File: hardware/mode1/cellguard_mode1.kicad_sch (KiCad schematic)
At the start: 22 parts, among them J1 Raspberry Pi 5 GPIO Header, J2 ZY12PDN PD Trigger (5V), J3 ATORCH BW150 부하 입력, K1 4CH Relay [SZH-RLBG-012], U1 INA226 [VLT-VCM029], U2 Battery Babysitter [PRT-13777], U3 MLX90614 #1 (0x5A, 셀 중앙), U4 ADS1115 [VLT-AD004], U5 DS18B20 #1 (셀 하단), U6 OLED 0.96in SPI [CN0219], U7 DS18B20 #2 (셀 중앙), U8 DS18B20 #3 (셀 상단·단자쪽), U9 MLX90614 #2 (0x5B, 셀 단자쪽)

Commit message: fix(hw): 모드 1 회로에서 F1 폴리퓨즈 제거 — 과전류 보호를 셀 보호회로에 위임
F1은 회로도를 그리며 넣은 부품인데 PLAN.md의 구매 확정 목록에도,
미확보 목록에도 없었다("퓨즈" 0건). 새로 사지 않고 회로에서 뺀다.

회로 (정본)
- gen_mode1_sch.py: POLYFUSE 심볼·F1 인스턴스 삭제. CELL_P_F 네트가
  사라지고 셀 +는 CELL_P 한 노드로 INA226 IN-·VBUS에 직결된다.
- 재생성 후 ERC 위반 0건, SVG 재출력. 네트리스트로 CELL_P = BT1.+ /
  U1.IN- / U1.VBUS 확인, CELL_P_F 0건 확인.

이 결정의 대가 — 회로 안에 과전류를 막을 소자가 하나도 없다
- 가이드 §3에 `⑥ 셀에 보호회로(PCM)가 붙어 있는가` 추가 (5가지 -> 6가지).
  protected/unprotected 구분법(18650 68~70mm vs 65mm, 파우치의 기판 유무),
  없으면 셀 교체 또는 폴리퓨즈 신규 구매.
- §5 3단계 셀 삽입 직전 검사에 보호회로 확인 추가.
- §7에 14번 "보호회로 없는 맨 셀을 물림" 추가 (13가지 -> 14가지).
- §2 BT1 행, §4-3 전력 경로에 경고 명시.

문서 정리
- §1 전류 경로 그림 2장에서 F1 제거. §4-3 CELL_P/CELL_P_F 두 행을 한 행으로.
  §9 폴리퓨즈 항목 삭제. §10 인계 목록에 보호회로 유무·실측 길이 추가.
- 백엔드 스펙 §3-5의 "퓨즈 앞" 표현 정정.
- CLAUDE.md: 직전 커밋에 넣은 "VBUS는 퓨즈 앞" 항목을 무퓨즈 정책으로 교체.
- PLAN.md: 변경 이력 2026-07-28 항목 신설, 하드웨어 제약에 무퓨즈 명시.

미해결 (PLAN.md `정의 필요`로 등록)
- 구매한 18650[ZM18650-2600-KC01]·리튬폴리머[TW102050]에 보호회로가
  실제로 있는지 실물 미확인. 없으면 이 결정의 전제가 깨진다.
- 보호회로가 있으면 18650이 68~70mm라 홀더 규격과 §4-5 DS18B20 3점
  배치 치수가 달라진다.

Co-Authored-By: Claude Opus 5 <noreply@anthropic.com>
Claude-Session: https://claude.ai/code/session_01JTJvnafHr2vM6f9oKrnscb
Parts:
- removed F1: PolyFuse 3A, symbol cellguard:POLYFUSE
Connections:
- net CELL_P_F is gone; now on net CELL_P: U1.2 (IN-)
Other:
- note added: "18650 홀더, JST 2.0 커넥터, 4.7k/10k 저항,"
- note added: "[!] 직렬 퓨즈 없음. 과전류 보호는 셀에 붙은 보호회로(PCM)에만 의존한다."
- note added: "보호회로 없는 맨 셀(unprotected)을 물리면 배선 단락 시 아무 보호도 없다 — 실물 확인 필수."
- note added: "충전: ZY12PDN 5V -[CH1]- Babysitter VIN -> (BQ24075) -> BAT+ -[CH3]- INA226 션트 - 셀 +"
- note removed: "전압 탭: INA226 VBUS는 퓨즈 앞(CELL_P)에서 딴다. 퓨즈 뒤면 폴리퓨즈 저항만큼 깎인다."
- note removed: "충전: ZY12PDN 5V -[CH1]- Babysitter VIN -> (BQ24075) -> BAT+ -[CH3]- INA226 션트 - F1 - 셀 +"
- note removed: "폴리퓨즈 3A, 18650 홀더, JST 2.0 커넥터, 4.7k/10k 저항,"
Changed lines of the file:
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@@
-	)
-	(symbol
-		(lib_id "cellguard:POLYFUSE")
-		(at 62.23 72.39 0)
-		(unit 1)
-		(exclude_from_sim no)
-		(in_bom yes)
-		(on_board yes)
-		(dnp no)
-		(property "Reference" "F1" (at 52.07 63.50 0) (effects (font (face "Apple SD Gothic Neo") (size 1.27 1.27)) (justify left bottom)))
-		(property "Value" "PolyFuse 3A" (at 52.07 66.04 0) (effects (font (face "Apple SD Gothic Neo") (size 1.27 1.27)) (justify left bottom)))
-		(property "Footprint" "" (at 62.23 72.39 0) (effects (font (face "Apple SD Gothic Neo") (size 1.27 1.27)) (hide yes)))
-		(property "Datasheet" "" (at 62.23 72.39 0) (effects (font (face "Apple SD Gothic Neo") (size 1.27 1.27)) (hide yes)))
-		(property "Description" "셀 + 경로 과전류 보호 (미확보 — 조립 전 확보 필요)" (at 62.23 72.39 0) (effects (font (face "Apple SD Gothic Neo") (size 1.27 1.27)) (hide yes)))
-		(instances
-			(project "cellguard_mode1"
-				(path "/2591c9a4-08c7-5581-87ba-34dbe85f198c" (reference "F1") (unit 1))
-			)
-		)
-	)
-	(wire
-		(pts (xy 46.99 72.39) (xy 41.91 72.39))
-		(stroke (width 0) (type default))
-	)
-	(global_label "CELL_P"
-		(shape bidirectional)
-		(at 41.91 72.39 180)
-		(effects (font (face "Apple SD Gothic Neo") (size 1.27 1.27)) (justify right))
-		(property "Intersheetrefs" "${INTERSHEET_REFS}" (at 0 0 0) (effects (font (face "Apple SD Gothic Neo") (size 1.27 1.27)) (hide yes)))
-	)
-	(wire
-		(pts (xy 77.47 72.39) (xy 82.55 72.39))
-		(stroke (width 0) (type default))
-	)
-	(global_label "CELL_P_F"
-		(shape bidirectional)
-		(at 82.55 72.39 0)
-		(effects (font (face "Apple SD Gothic Neo") (size 1.27 1.27)) (justify left))
-		(property "Intersheetrefs" "${INTERSHEET_REFS}" (at 0 0 0) (effects (font (face "Apple SD Gothic Neo") (size 1.27 1.27)) (hide yes)))
 	)
 	(symbol
@@
 		(stroke (width 0) (type default))
 	)
-	(global_label "CELL_P_F"
+	(global_label "CELL_P"
 		(shape bidirectional)
 		(at 35.56 113.03 180)
@@
 		(effects (font (face "Apple SD Gothic Neo") (size 3.0 3.0)) (justify left bottom))
 	)
-	(text "충전:  ZY12PDN 5V -[CH1]- Babysitter VIN -> (BQ24075) -> BAT+ -[CH3]- INA226 션트 - F1 - 셀 +"
+	(text "충전:  ZY12PDN 5V -[CH1]- Babysitter VIN -> (BQ24075) -> BAT+ -[CH3]- INA226 션트 - 셀 +"
 		(exclude_from_sim no)
 		(at 20.00 314.00 0)
 		(effects (font (face "Apple SD Gothic Neo") (size 2.0 2.0)) (justify left bottom))
 	)
-	(text "전압 탭:  INA226 VBUS는 퓨즈 앞(CELL_P)에서 딴다. 퓨즈 뒤면 폴리퓨즈 저항만큼 깎인다."
+	(text "[!] 직렬 퓨즈 없음.  과전류 보호는 셀에 붙은 보호회로(PCM)에만 의존한다."
 		(exclude_from_sim no)
 		(at 20.00 319.20 0)
 		(effects (font (face "Apple SD Gothic Neo") (size 2.0 2.0)) (justify left bottom))
 	)
+	(text "    보호회로 없는 맨 셀(unprotected)을 물리면 배선 단락 시 아무 보호도 없다 — 실물 확인 필수."
+		(exclude_from_sim no)
+		(at 20.00 324.40 0)
+		(effects (font (face "Apple SD Gothic Neo") (size 2.0 2.0)) (justify left bottom))
+	)
 	(text "방전:  셀 + -> ... -> Babysitter SYS+ -[CH2]- ATORCH BW150 부하 +"
 		(exclude_from_sim no)
-		(at 20.00 324.40 0)
+		(at 20.00 329.60 0)
 		(effects (font (face "Apple SD Gothic Neo") (size 2.0 2.0)) (justify left bottom))
 	)
 	(text "부호 규약:  INA226 IN+ -> IN- 방향(릴레이 -> 셀)이 양수 = 충전.  방전은 음수."
 		(exclude_from_sim no)
-		(at 20.00 329.60 0)
+		(at 20.00 334.80 0)
 		(effects (font (face "Apple SD Gothic Neo") (size 2.0 2.0)) (justify left bottom))
 	)
 	(text "[!] 조립 전 반드시 확인 — 여기서 틀리면 부품이 탄다"
 		(exclude_from_sim no)
-		(at 20.00 337.80 0)
+		(at 20.00 343.00 0)
 		(effects (font (face "Apple SD Gothic Neo") (size 2.5 2.5)) (justify left bottom))
 	)
 	(text "1. ZY12PDN을 5V로 설정했는가.  9V/12V면 Babysitter가 즉시 파손된다."
 		(exclude_from_sim no)
-		(at 20.00 345.80 0)
+		(at 20.00 351.00 0)
 		(effects (font (face "Apple SD Gothic Neo") (size 2.0 2.0)) (justify left bottom))
 	)
 	(text "2. 릴레이 VCC-JD_VCC 점퍼를 뽑았는가.  VCC=Pi 3.3V(옵토측), JD_VCC=5V(코일측)."
 		(exclude_from_sim no)
-		(at 20.00 351.00 0)
+		(at 20.00 356.20 0)
 		(effects (font (face "Apple SD Gothic Neo") (size 2.0 2.0)) (justify left bottom))
 	)
 	(text "   점퍼를 꽂아 두면 VCC=5V가 되어 3.3V 로직으로 옵토 LED를 확실히 끄지 못한다."
 		(exclude_from_sim no)
-		(at 20.00 356.20 0)
+		(at 20.00 361.40 0)
 		(effects (font (face "Apple SD Gothic Neo") (size 2.0 2.0)) (justify left bottom))
 	)
 	(text "3. INA226 보드의 션트 저항값을 실크스크린에서 읽었는가."
 		(exclude_from_sim no)
-		(at 20.00 361.40 0)
+		(at 20.00 366.60 0)
 		(effects (font (face "Apple SD Gothic Neo") (size 2.0 2.0)) (justify left bottom))
 	)
 	(text "   R100=0.1ohm / R010=0.01ohm / R002=0.002ohm -> Calibration 레지스터 값이 달라진다."
 		(exclude_from_sim no)
-		(at 20.00 366.60 0)
+		(at 20.00 371.80 0)
 		(effects (font (face "Apple SD Gothic Neo") (size 2.0 2.0)) (justify left bottom))
 	)
 	(text "   전류 측정 상한은 션트가 아니라 16비트 Current 레지스터가 정한다 -> 기본 설정에서 3.28A."
 		(exclude_from_sim no)
-		(at 20.00 371.80 0)
+		(at 20.00 377.00 0)
 		(effects (font (face "Apple SD Gothic Neo") (size 2.0 2.0)) (justify left bottom))
 	)
 	(text "4. 셀 -(음극)를 시스템 GND에 직접 연결하지 마라."
 		(exclude_from_sim no)
-		(at 20.00 377.00 0)
+		(at 20.00 382.20 0)
 		(effects (font (face "Apple SD Gothic Neo") (size 2.0 2.0)) (justify left bottom))
 	)
 	(text "   CELL_N은 Babysitter BAT- 하나에만 간다. BQ27441의 20mohm 센스 저항이"
 		(exclude_from_sim no)
-		(at 20.00 382.20 0)
+		(at 20.00 387.40 0)
 		(effects (font (face "Apple SD Gothic Neo") (size 2.0 2.0)) (justify left bottom))
 	)
 	(text "   BAT-와 GND 사이에 있어서, 직결하면 이 저항이 단락되고 SOC가 안 나온다."
 		(exclude_from_sim no)
-		(at 20.00 387.40 0)
+		(at 20.00 392.60 0)
 		(effects (font (face "Apple SD Gothic Neo") (size 2.0 2.0)) (justify left bottom))
 	)
 	(text "[!] 릴레이는 active-LOW다"
 		(exclude_from_sim no)
-		(at 20.00 395.60 0)
+		(at 20.00 400.80 0)
 		(effects (font (face "Apple SD Gothic Neo") (size 2.5 2.5)) (justify left bottom))
 	)
 	(text "GPIO=0 -> 접점 붙음(도통) / GPIO=1 -> 접점 떨어짐(차단)."
 		(exclude_from_sim no)
-		(at 20.00 403.60 0)
+		(at 20.00 408.80 0)
 		(effects (font (face "Apple SD Gothic Neo") (size 2.0 2.0)) (justify left bottom))
 	)
 	(text "모든 배터리 경로가 NO 접점을 지나므로 정전 / 부팅 중 / 크래시 = 자동 차단(fail-safe)."
 		(exclude_from_sim no)
-		(at 20.00 408.80 0)
+		(at 20.00 414.00 0)
 		(effects (font (face "Apple SD Gothic Neo") (size 2.0 2.0)) (justify left bottom))
 	)
 	(text "부팅 초기 보호 2중화:  IN1~IN4에 10k 풀업(R3~R6)"
 		(exclude_from_sim no)
-		(at 20.00 414.00 0)
+		(at 20.00 419.20 0)
 		(effects (font (face "Apple SD Gothic Neo") (size 2.0 2.0)) (justify left bottom))
 	)
 	(text "                        + /boot/firmware/config.txt 에 gpio=5,6,13,19=op,dh"
 		(exclude_from_sim no)
-		(at 20.00 419.20 0)
+		(at 20.00 424.40 0)
 		(effects (font (face "Apple SD Gothic Neo") (size 2.0 2.0)) (justify left bottom))
 	)
 	(text "  ※ config.txt 쪽은 Pi 5 에서 안 먹을 수 있다. 전원 인가 순간부터 확실한 건 10k 풀업뿐이니"
 		(exclude_from_sim no)
-		(at 20.00 424.40 0)
+		(at 20.00 429.60 0)
 		(effects (font (face "Apple SD Gothic Neo") (size 2.0 2.0)) (justify left bottom))
 	)
 	(text "     R3~R6 을 절대 생략하지 마라.  재부팅 후 pinctrl get 5,6,13,19 으로 확인할 것."
 		(exclude_from_sim no)
-		(at 20.00 429.60 0)
+		(at 20.00 434.80 0)
 		(effects (font (face "Apple SD Gothic Neo") (size 2.0 2.0)) (justify left bottom))
 	)
@@
 		(effects (font (face "Apple SD Gothic Neo") (size 2.5 2.5)) (justify left bottom))
 	)
-	(text "폴리퓨즈 3A, 18650 홀더, JST 2.0 커넥터, 4.7k/10k 저항,"
+	(text "18650 홀더, JST 2.0 커넥터, 4.7k/10k 저항,"
 		(exclude_from_sim no)
 		(at 580.00 408.80 0)

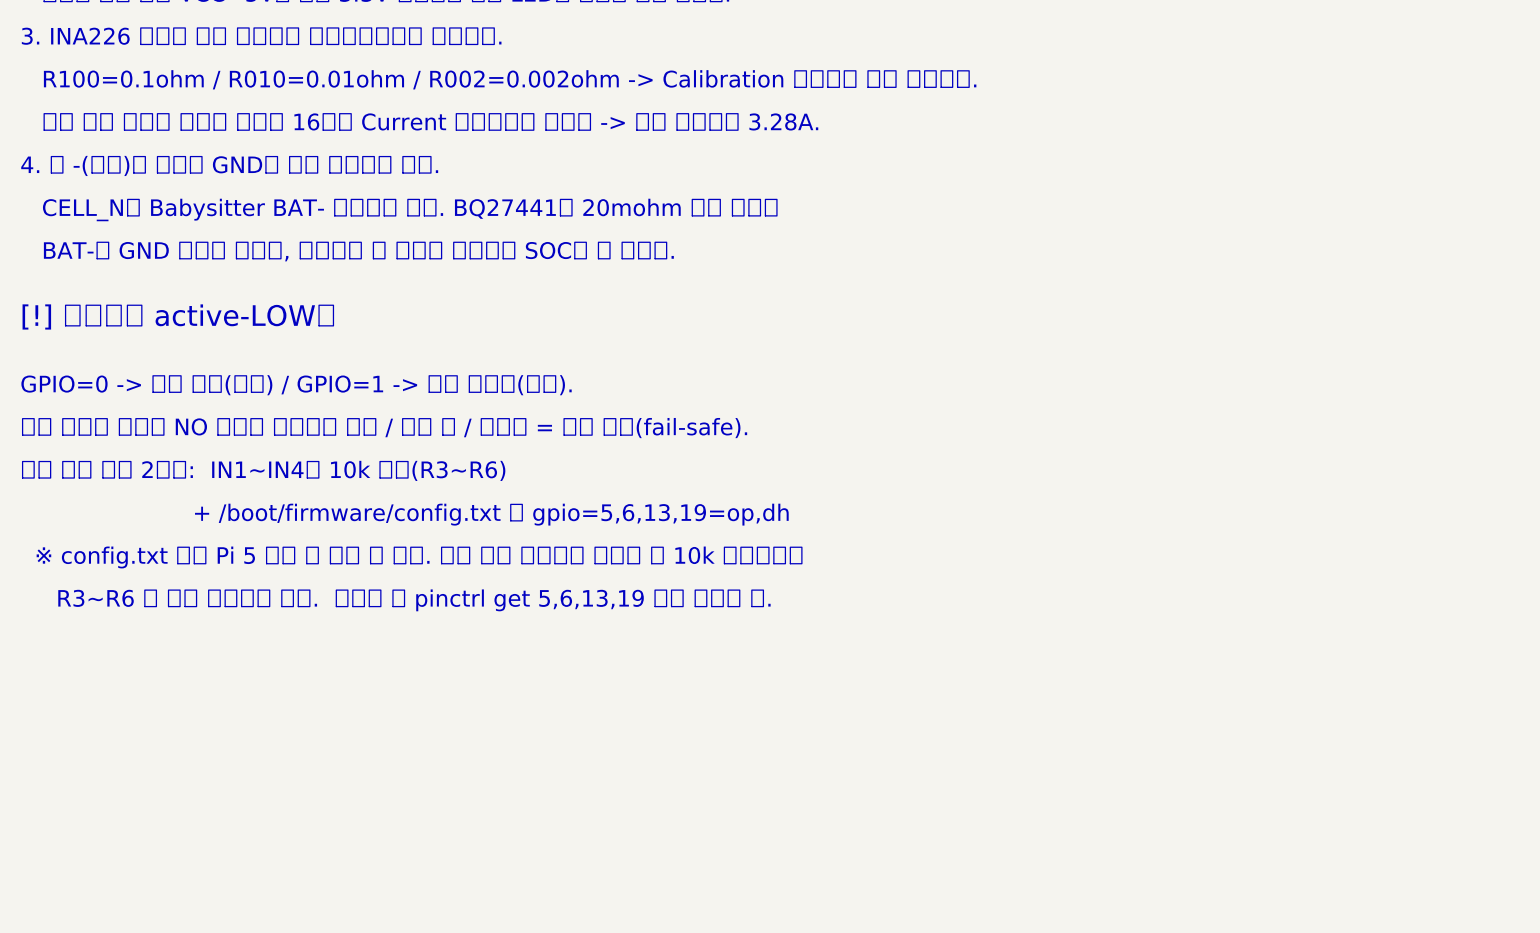
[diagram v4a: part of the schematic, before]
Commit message: docs(hw): SparkFun 공식 회로도로 Babysitter 관련 오류 3건 정정
`bq24075` 데이터시트와 Battery Babysitter v10 공식 회로도를 대조한 결과,
문서가 사실과 다른 곳이 세 군데 있었다.

1. 센스 저항 위치가 반대였다
   `R11`(0.01Ω)은 배터리 `−`↔GND가 아니라 배터리 `+` 쪽 하이사이드
   (`BATTERY_IN`↔`V_BATT`)에 있고, 배터리 `−`는 보드 `GND`에 직결이다.
   - "셀 −를 GND에 물리면 SOC가 죽는다" → 사실 아님. `CELL_N`↔GND 도통은 정상
   - STEP 24의 `CELL_N` 격리 도통 검사는 멀쩡한 배선을 불합격시킨다 → 육안 검사로 교체
   - 백엔드 스펙 §3-5의 `voltage_v` 20mΩ 보정식은 없는 오차를 3A에서 60mV씩
     주입한다 → 폐기. 남는 건 배선 IR 강하뿐이라 계산 보정 불가
   - `CELL_N`을 한 점에만 무는 규칙 자체는 유지(스타 그라운드). 배선 변경 없음
   - §13 H5를 "센스 저항 역산"에서 "귀환 경로 IR 강하 실측"으로 교체

2. 보드 실크스크린이 회로도 네트 이름과 같다는 기록이 틀렸다
   `GND_IN`·`SYS+`·`SYS−`·`BAT+`·`BAT−`는 보드에 없는 글자다.
   STEP 3에 대응표 추가 — `VIN −` / `VOUT +` / `VOUT −` / JST `+` / JST `−`,
   네모 패드가 있는 줄이 `+`, 한 줄의 3구멍은 같은 네트(`JP2~4`·`JP7~9` 병렬).
   `GND`·`GND_IN`·`SYS−`가 보드 안에서 같은 네트임도 명시.

3. 온보드 스위치 2개가 가이드에 아예 없었다 (§2-⑥ 신설)
   - `S1` 슬라이드 = `SYSOFF`(active-high, HIGH=OFF) — `OFF`면 `SYS+` 출력 0
   - `S2` DIP = `EN1`/`EN2`, 10k로 `OUT` 풀업 — 출고 기본 `1,1`은 Standby(충전 안 함).
     설정값 `EN2=1, EN1=0`
   - `R5`=590Ω → `I_CHG`≈1.5A, `R7`=1.1kΩ → `I_INMAX`≈1.5A.
     2550mAh 18650에 0.59C라 셀 스펙 확인 항목 추가

회로도 심볼 설명과 주석에도 반영하고 재생성(ERC 위반 0건).

Co-Authored-By: Claude Opus 5 <noreply@anthropic.com>
Claude-Session: https://claude.ai/code/session_01TdBrQJ3tYNhWGCkoy4xU7s
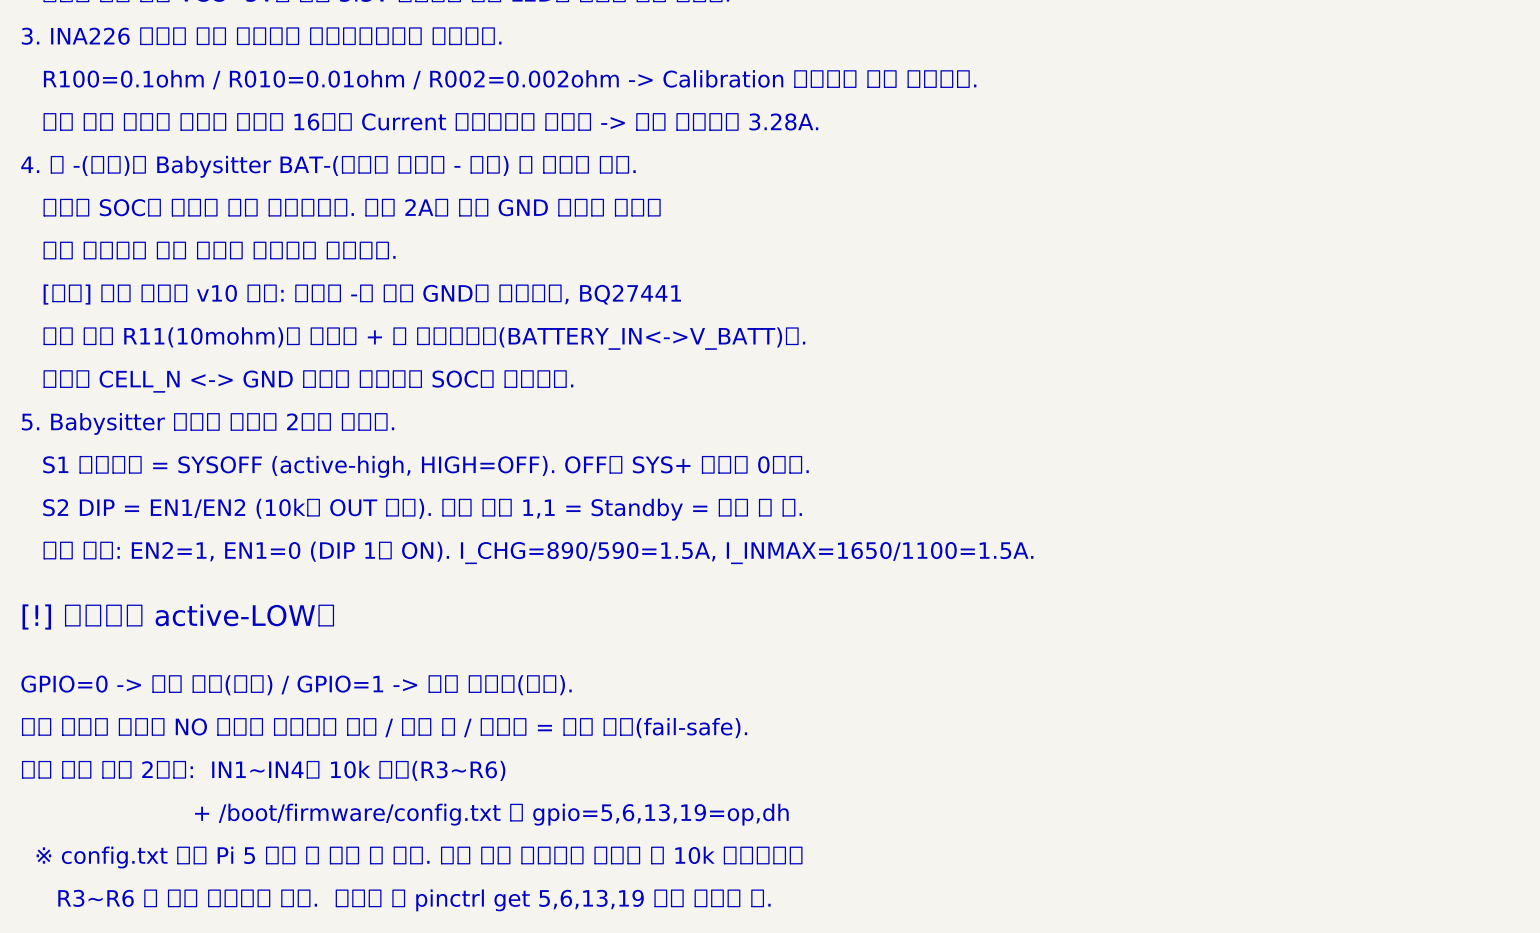
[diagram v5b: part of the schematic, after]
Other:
- note added: "4. 셀 -(음극)는 Babysitter BAT-(보드의 배터리 - 단자) 한 점에만 문다."
- note added: "5. Babysitter 온보드 스위치 2개를 맞춰라."
- note added: "S1 슬라이드 = SYSOFF (active-high, HIGH=OFF). OFF면 SYS+ 출력이 0이다."
- note added: "S2 DIP = EN1/EN2 (10k로 OUT 풀업). 출고 기본 1,1 = Standby = 충전 안 함."
- note added: "[주의] 공식 회로도 v10 확인: 배터리 -는 보드 GND에 직결이고, BQ27441"
- note added: "따라서 CELL_N <-> GND 도통은 정상이며 SOC와 무관하다."
- note added: "센스 저항 R11(10mohm)은 배터리 + 쪽 하이사이드(BATTERY_IN<->V_BATT)다."
- note added: "우리 설정: EN2=1, EN1=0 (DIP 1만 ON). I_CHG=890/590=1.5A, I_INMAX=1650/1100=1.5A."
- note added: "이유는 SOC가 아니라 스타 그라운드다. 방전 2A가 신호 GND 레일을 지나면"
- note added: "전압 강하만큼 모든 센서의 기준점이 흔들린다."
- note removed: "4. 셀 -(음극)를 시스템 GND에 직접 연결하지 마라."
- note removed: "BAT-와 GND 사이에 있어서, 직결하면 이 저항이 단락되고 SOC가 안 나온다."
- note removed: "CELL_N은 Babysitter BAT- 하나에만 간다. BQ27441의 20mohm 센스 저항이"
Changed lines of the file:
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@@
 		(property "Footprint" "" (at 219.71 167.64 0) (effects (font (face "Apple SD Gothic Neo") (size 1.27 1.27)) (hide yes)))
 		(property "Datasheet" "" (at 219.71 167.64 0) (effects (font (face "Apple SD Gothic Neo") (size 1.27 1.27)) (hide yes)))
-		(property "Description" "BQ24075 충전기 + BQ27441 퓨얼게이지(SOC), I2C 0x55" (at 219.71 167.64 0) (effects (font (face "Apple SD Gothic Neo") (size 1.27 1.27)) (hide yes)))
+		(property "Description" "BQ24075 충전기 + BQ27441 퓨얼게이지(SOC), I2C 0x55. 핀 이름은 회로도 규약이며 보드 실크스크린과 다르다 -- VIN/GND_IN=VIN +/-, SYS+/SYS-=VOUT +/-, BAT+/BAT-=JST +/-. GND/GND_IN/SYS-는 보드 안에서 같은 GND 네트" (at 219.71 167.64 0) (effects (font (face "Apple SD Gothic Neo") (size 1.27 1.27)) (hide yes)))
 		(instances
 			(project "cellguard_mode1"
@@
 		(effects (font (face "Apple SD Gothic Neo") (size 2.0 2.0)) (justify left bottom))
 	)
-	(text "4. 셀 -(음극)를 시스템 GND에 직접 연결하지 마라."
+	(text "4. 셀 -(음극)는 Babysitter BAT-(보드의 배터리 - 단자) 한 점에만 문다."
 		(exclude_from_sim no)
 		(at 20.00 382.20 0)
 		(effects (font (face "Apple SD Gothic Neo") (size 2.0 2.0)) (justify left bottom))
 	)
-	(text "   CELL_N은 Babysitter BAT- 하나에만 간다. BQ27441의 20mohm 센스 저항이"
+	(text "   이유는 SOC가 아니라 스타 그라운드다. 방전 2A가 신호 GND 레일을 지나면"
 		(exclude_from_sim no)
 		(at 20.00 387.40 0)
 		(effects (font (face "Apple SD Gothic Neo") (size 2.0 2.0)) (justify left bottom))
 	)
-	(text "   BAT-와 GND 사이에 있어서, 직결하면 이 저항이 단락되고 SOC가 안 나온다."
+	(text "   전압 강하만큼 모든 센서의 기준점이 흔들린다."
 		(exclude_from_sim no)
 		(at 20.00 392.60 0)
 		(effects (font (face "Apple SD Gothic Neo") (size 2.0 2.0)) (justify left bottom))
 	)
+	(text "   [주의] 공식 회로도 v10 확인: 배터리 -는 보드 GND에 직결이고, BQ27441"
+		(exclude_from_sim no)
+		(at 20.00 397.80 0)
+		(effects (font (face "Apple SD Gothic Neo") (size 2.0 2.0)) (justify left bottom))
+	)
+	(text "   센스 저항 R11(10mohm)은 배터리 + 쪽 하이사이드(BATTERY_IN<->V_BATT)다."
+		(exclude_from_sim no)
+		(at 20.00 403.00 0)
+		(effects (font (face "Apple SD Gothic Neo") (size 2.0 2.0)) (justify left bottom))
+	)
+	(text "   따라서 CELL_N <-> GND 도통은 정상이며 SOC와 무관하다."
+		(exclude_from_sim no)
+		(at 20.00 408.20 0)
+		(effects (font (face "Apple SD Gothic Neo") (size 2.0 2.0)) (justify left bottom))
+	)
+	(text "5. Babysitter 온보드 스위치 2개를 맞춰라."
+		(exclude_from_sim no)
+		(at 20.00 413.40 0)
+		(effects (font (face "Apple SD Gothic Neo") (size 2.0 2.0)) (justify left bottom))
+	)
+	(text "   S1 슬라이드 = SYSOFF (active-high, HIGH=OFF). OFF면 SYS+ 출력이 0이다."
+		(exclude_from_sim no)
+		(at 20.00 418.60 0)
+		(effects (font (face "Apple SD Gothic Neo") (size 2.0 2.0)) (justify left bottom))
+	)
+	(text "   S2 DIP = EN1/EN2 (10k로 OUT 풀업). 출고 기본 1,1 = Standby = 충전 안 함."
+		(exclude_from_sim no)
+		(at 20.00 423.80 0)
+		(effects (font (face "Apple SD Gothic Neo") (size 2.0 2.0)) (justify left bottom))
+	)
+	(text "   우리 설정: EN2=1, EN1=0 (DIP 1만 ON). I_CHG=890/590=1.5A, I_INMAX=1650/1100=1.5A."
+		(exclude_from_sim no)
+		(at 20.00 429.00 0)
+		(effects (font (face "Apple SD Gothic Neo") (size 2.0 2.0)) (justify left bottom))
+	)
 	(text "[!] 릴레이는 active-LOW다"
 		(exclude_from_sim no)
-		(at 20.00 400.80 0)
+		(at 20.00 437.20 0)
 		(effects (font (face "Apple SD Gothic Neo") (size 2.5 2.5)) (justify left bottom))
 	)
 	(text "GPIO=0 -> 접점 붙음(도통) / GPIO=1 -> 접점 떨어짐(차단)."
 		(exclude_from_sim no)
-		(at 20.00 408.80 0)
+		(at 20.00 445.20 0)
 		(effects (font (face "Apple SD Gothic Neo") (size 2.0 2.0)) (justify left bottom))
 	)
 	(text "모든 배터리 경로가 NO 접점을 지나므로 정전 / 부팅 중 / 크래시 = 자동 차단(fail-safe)."
 		(exclude_from_sim no)
-		(at 20.00 414.00 0)
+		(at 20.00 450.40 0)
 		(effects (font (face "Apple SD Gothic Neo") (size 2.0 2.0)) (justify left bottom))
 	)
 	(text "부팅 초기 보호 2중화:  IN1~IN4에 10k 풀업(R3~R6)"
 		(exclude_from_sim no)
-		(at 20.00 419.20 0)
+		(at 20.00 455.60 0)
 		(effects (font (face "Apple SD Gothic Neo") (size 2.0 2.0)) (justify left bottom))
 	)
 	(text "                        + /boot/firmware/config.txt 에 gpio=5,6,13,19=op,dh"
 		(exclude_from_sim no)
-		(at 20.00 424.40 0)
+		(at 20.00 460.80 0)
 		(effects (font (face "Apple SD Gothic Neo") (size 2.0 2.0)) (justify left bottom))
 	)
 	(text "  ※ config.txt 쪽은 Pi 5 에서 안 먹을 수 있다. 전원 인가 순간부터 확실한 건 10k 풀업뿐이니"
 		(exclude_from_sim no)
-		(at 20.00 429.60 0)
+		(at 20.00 466.00 0)
 		(effects (font (face "Apple SD Gothic Neo") (size 2.0 2.0)) (justify left bottom))
 	)
 	(text "     R3~R6 을 절대 생략하지 마라.  재부팅 후 pinctrl get 5,6,13,19 으로 확인할 것."
 		(exclude_from_sim no)
-		(at 20.00 434.80 0)
-		(effects (font (face "Apple SD Gothic Neo") (size 2.0 2.0)) (justify left bottom))
-	)
+		(at 20.00 471.20 0)
+		(effects (font (face "Apple SD Gothic Neo") (size 2.0 2.0)) (justify left bottom))
+	)
